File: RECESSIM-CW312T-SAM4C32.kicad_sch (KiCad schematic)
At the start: 2 parts

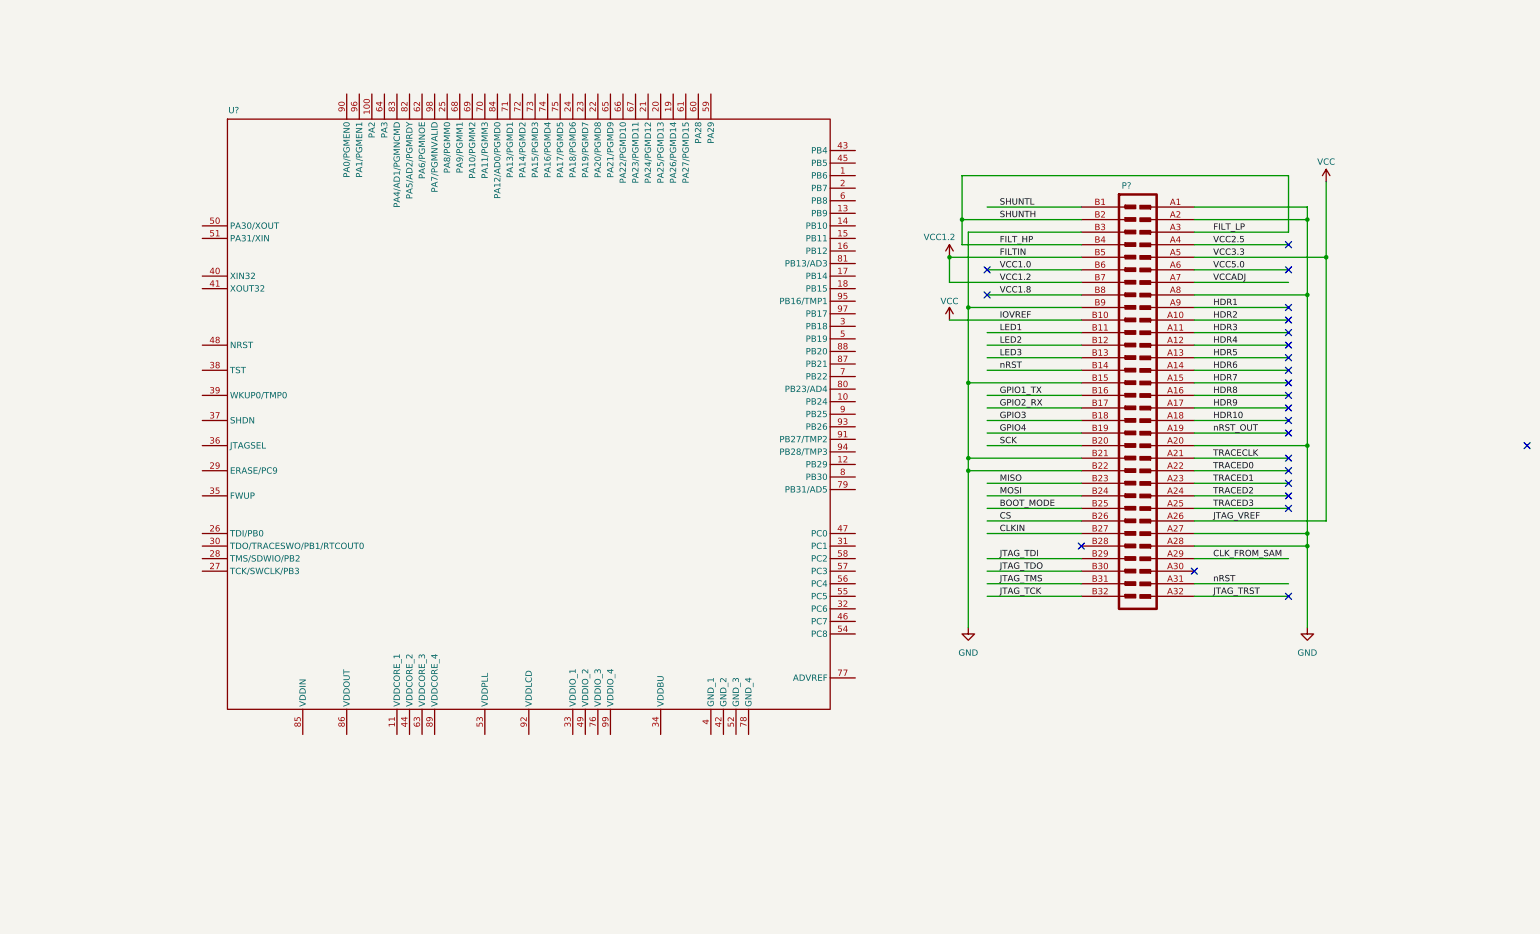
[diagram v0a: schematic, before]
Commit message: Added test points, power and JTAG connections
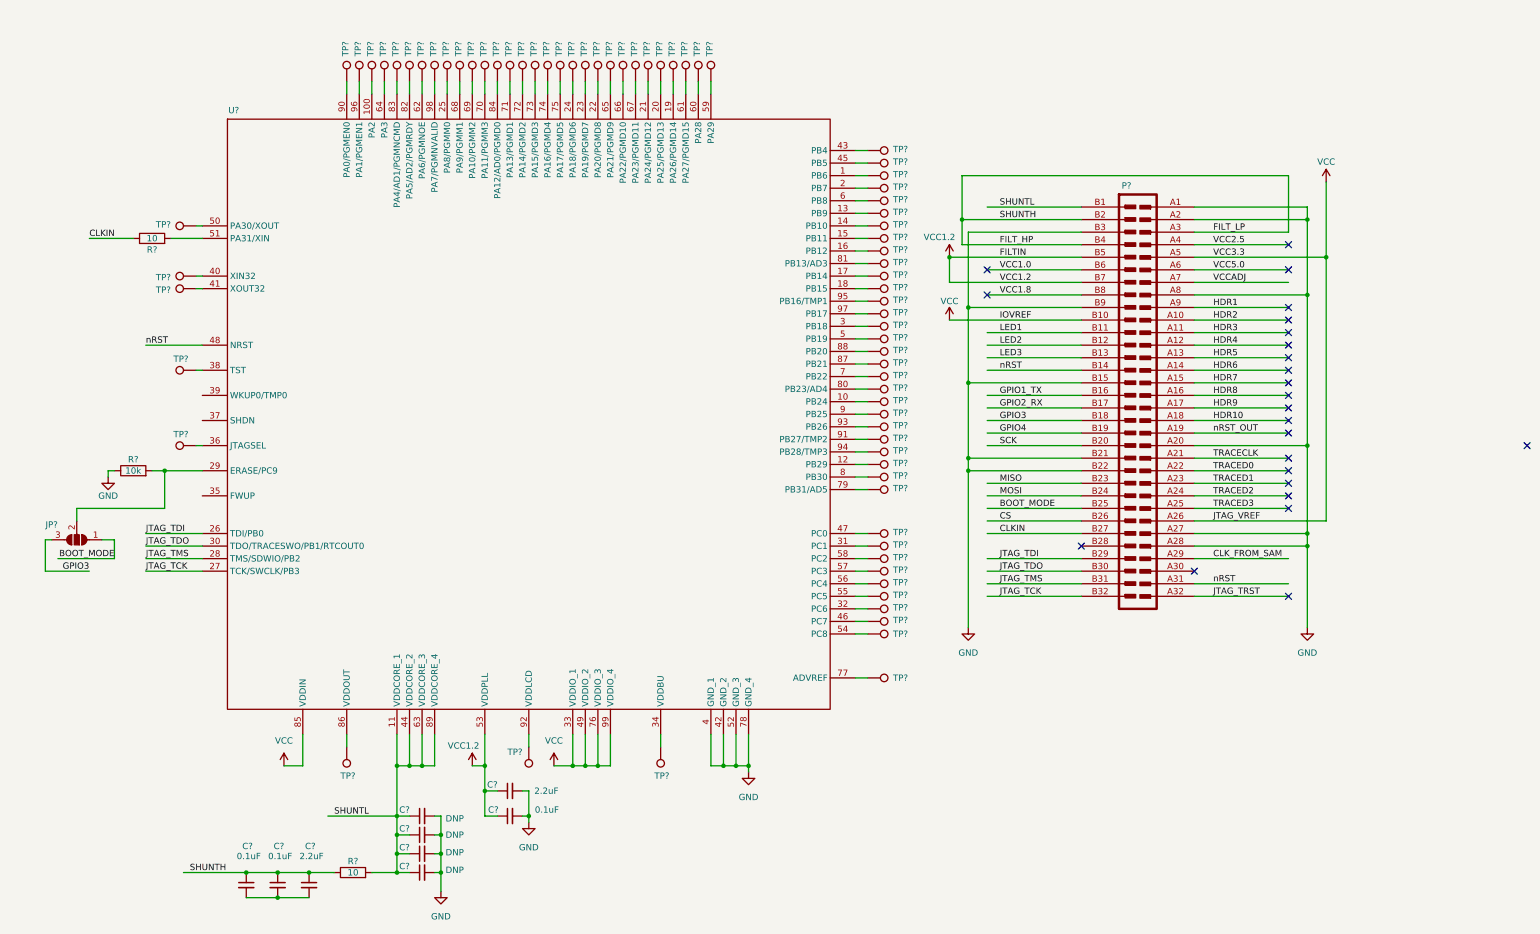
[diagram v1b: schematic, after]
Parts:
- added C? (x3): 0.1uF, symbol Device:C_Small
- added C? (x4): DNP, symbol Device:C_Small
- added C? (x2): 2.2uF, symbol Device:C_Small
- added JP?: SolderJumper_3_Open, symbol Jumper:SolderJumper_3_Open
- added R? (x2): 10, symbol Device:R
- added R?: 10k, symbol Device:R
- added TP? (x76): TestPoint, symbol Connector:TestPoint
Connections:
- net BOOT_MODE: now also JP?.1 (A)
- net CLKIN: now also R?.1
- net FILT_HP: now also C?.1, C?.1, C?.1, R?.1
- net GND: now also U?.4 (GND_1), U?.42 (GND_2), U?.52 (GND_3), U?.78 (GND_4), C?.2, C?.2, C?.2, C?.2, C?.2, C?.2, R?.1
- net GPIO3: now also JP?.3 (B)
- net JTAG_TCK: now also U?.27 (TCK/SWCLK/PB3)
- net JTAG_TDI: now also U?.26 (TDI/PB0)
- net JTAG_TDO: now also U?.30 (TDO/TRACESWO/PB1/RTCOUT0)
- net JTAG_TMS: now also U?.28 (TMS/SDWIO/PB2)
- net SHUNTL: now also U?.11 (VDDCORE_1), U?.44 (VDDCORE_2), U?.63 (VDDCORE_3), U?.89 (VDDCORE_4), C?.1, C?.1, C?.1, C?.1, R?.2
- net VCC: now also U?.33 (VDDIO_1), U?.49 (VDDIO_2), U?.76 (VDDIO_3), U?.85 (VDDIN), U?.99 (VDDIO_4)
- net VCC1.2: now also U?.53 (VDDPLL), C?.1, C?.1
- net nRST: now also U?.48 (NRST)
- net at U?.1 (PB6): now also TP?.1
- net at U?.10 (PB24): now also TP?.1
- net at U?.100 (PA2): now also TP?.1
- net at U?.12 (PB29): now also TP?.1
- net at U?.13 (PB9): now also TP?.1
- net at U?.14 (PB10): now also TP?.1
- net at U?.15 (PB11): now also TP?.1
- net at U?.16 (PB12): now also TP?.1
- net at U?.17 (PB14): now also TP?.1
- net at U?.18 (PB15): now also TP?.1
- net at U?.19 (PA26/PGMD14): now also TP?.1
- net at U?.2 (PB7): now also TP?.1
- net at U?.20 (PA25/PGMD13): now also TP?.1
- net at U?.21 (PA24/PGMD12): now also TP?.1
- net at U?.22 (PA20/PGMD8): now also TP?.1
- net at U?.23 (PA19/PGMD7): now also TP?.1
- net at U?.24 (PA18/PGMD6): now also TP?.1
- net at U?.25 (PA8/PGMM0): now also TP?.1
- net at U?.29 (ERASE/PC9): now also JP?.2 (C), R?.2
- net at U?.3 (PB18): now also TP?.1
- net at U?.31 (PC1): now also TP?.1
- net at U?.32 (PC6): now also TP?.1
- net at U?.34 (VDDBU): now also TP?.1
- net at U?.36 (JTAGSEL): now also TP?.1
- net at U?.38 (TST): now also TP?.1
- net at U?.40 (XIN32): now also TP?.1
- net at U?.41 (XOUT32): now also TP?.1
- net at U?.43 (PB4): now also TP?.1
- net at U?.45 (PB5): now also TP?.1
- net at U?.46 (PC7): now also TP?.1
- net at U?.47 (PC0): now also TP?.1
- net at U?.5 (PB19): now also TP?.1
- net at U?.50 (PA30/XOUT): now also TP?.1
- net at U?.51 (PA31/XIN): now also R?.2
- net at U?.54 (PC8): now also TP?.1
- net at U?.55 (PC5): now also TP?.1
- net at U?.56 (PC4): now also TP?.1
- net at U?.57 (PC3): now also TP?.1
- net at U?.58 (PC2): now also TP?.1
- net at U?.59 (PA29): now also TP?.1
- net at U?.6 (PB8): now also TP?.1
- net at U?.60 (PA28): now also TP?.1
- net at U?.61 (PA27/PGMD15): now also TP?.1
- net at U?.62 (PA6/PGMNOE): now also TP?.1
- net at U?.64 (PA3): now also TP?.1
- net at U?.65 (PA21/PGMD9): now also TP?.1
- net at U?.66 (PA22/PGMD10): now also TP?.1
- net at U?.67 (PA23/PGMD11): now also TP?.1
- net at U?.68 (PA9/PGMM1): now also TP?.1
- net at U?.69 (PA10/PGMM2): now also TP?.1
- net at U?.7 (PB22): now also TP?.1
- net at U?.70 (PA11/PGMM3): now also TP?.1
- net at U?.71 (PA13/PGMD1): now also TP?.1
- net at U?.72 (PA14/PGMD2): now also TP?.1
- net at U?.73 (PA15/PGMD3): now also TP?.1
- net at U?.74 (PA16/PGMD4): now also TP?.1
- net at U?.75 (PA17/PGMD5): now also TP?.1
- net at U?.77 (ADVREF): now also TP?.1
- net at U?.79 (PB31/AD5): now also TP?.1
- net at U?.8 (PB30): now also TP?.1
- net at U?.80 (PB23/AD4): now also TP?.1
- net at U?.81 (PB13/AD3): now also TP?.1
- net at U?.82 (PA5/AD2/PGMRDY): now also TP?.1
- net at U?.83 (PA4/AD1/PGMNCMD): now also TP?.1
- net at U?.84 (PA12/AD0/PGMD0): now also TP?.1
- net at U?.86 (VDDOUT): now also TP?.1
- net at U?.87 (PB21): now also TP?.1
- net at U?.88 (PB20): now also TP?.1
- net at U?.9 (PB25): now also TP?.1
- net at U?.90 (PA0/PGMEN0): now also TP?.1
- net at U?.91 (PB27/TMP2): now also TP?.1
- net at U?.92 (VDDLCD): now also TP?.1
- net at U?.93 (PB26): now also TP?.1
- net at U?.94 (PB28/TMP3): now also TP?.1
- net at U?.95 (PB16/TMP1): now also TP?.1
- net at U?.96 (PA1/PGMEN1): now also TP?.1
- net at U?.97 (PB17): now also TP?.1
- net at U?.98 (PA7/PGMNVALID): now also TP?.1
- new net: C?.2, C?.2, C?.2

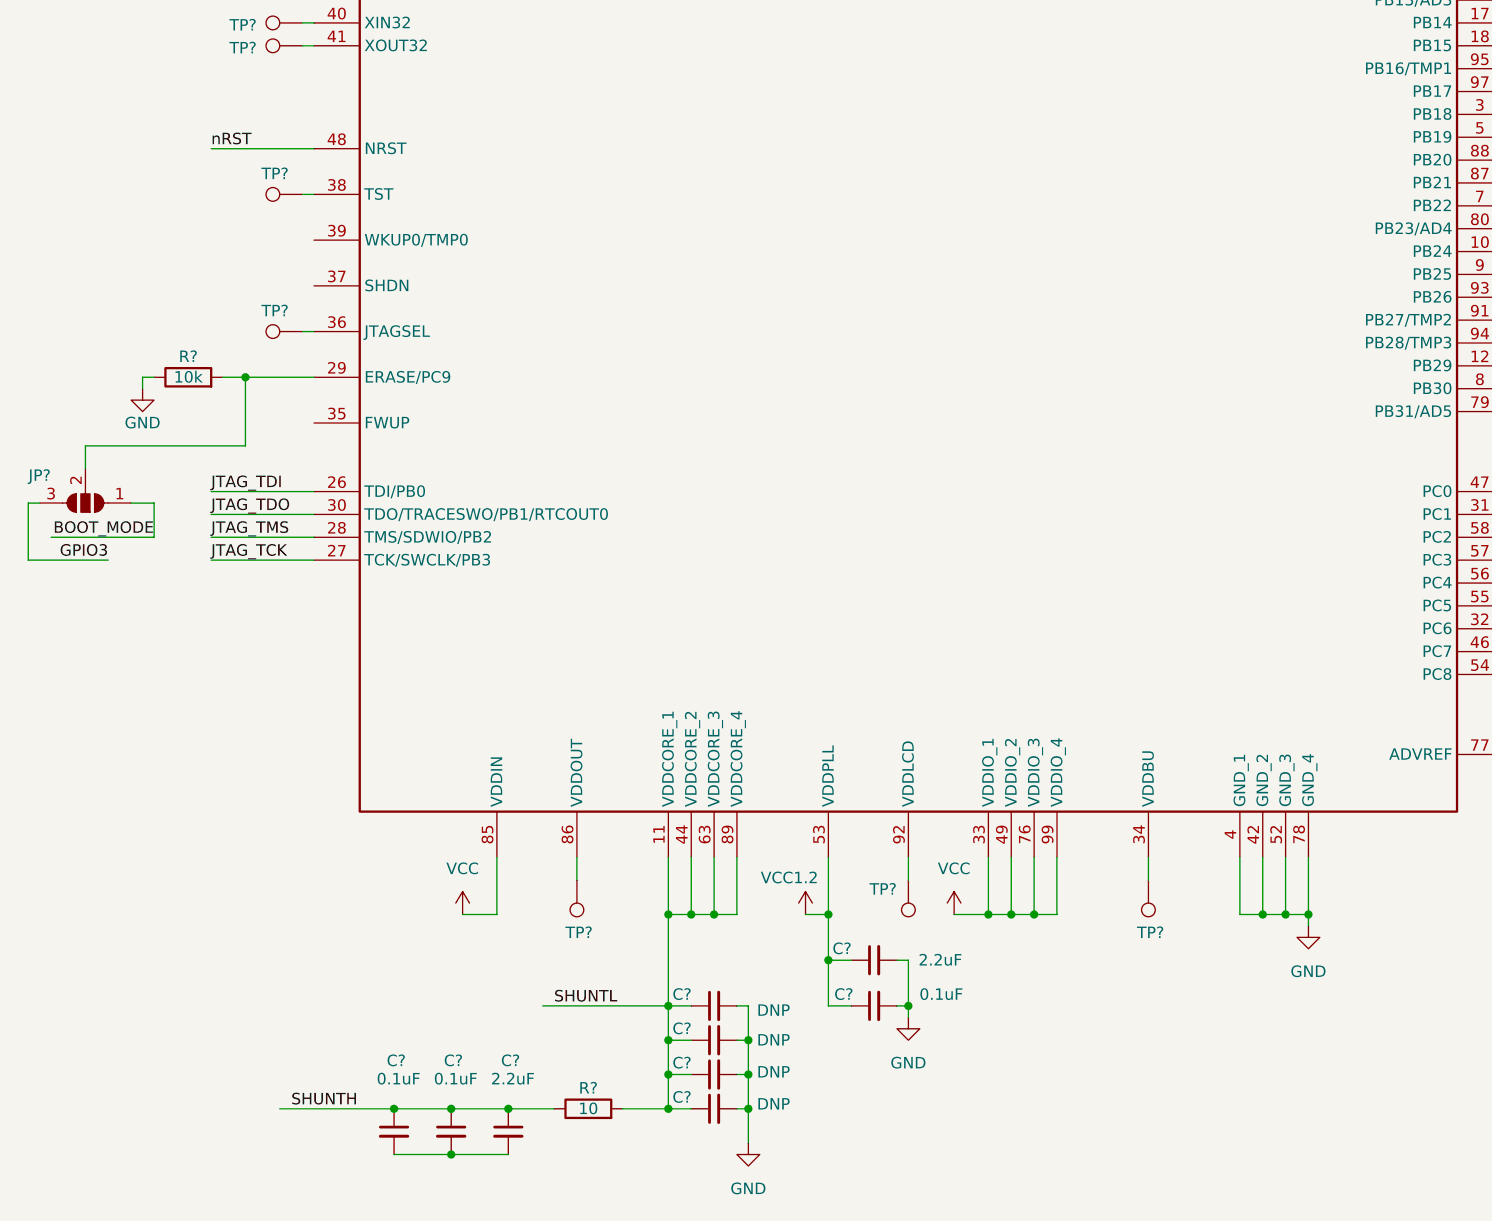
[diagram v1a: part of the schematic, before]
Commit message: Connected VDDBU to power, added more test points
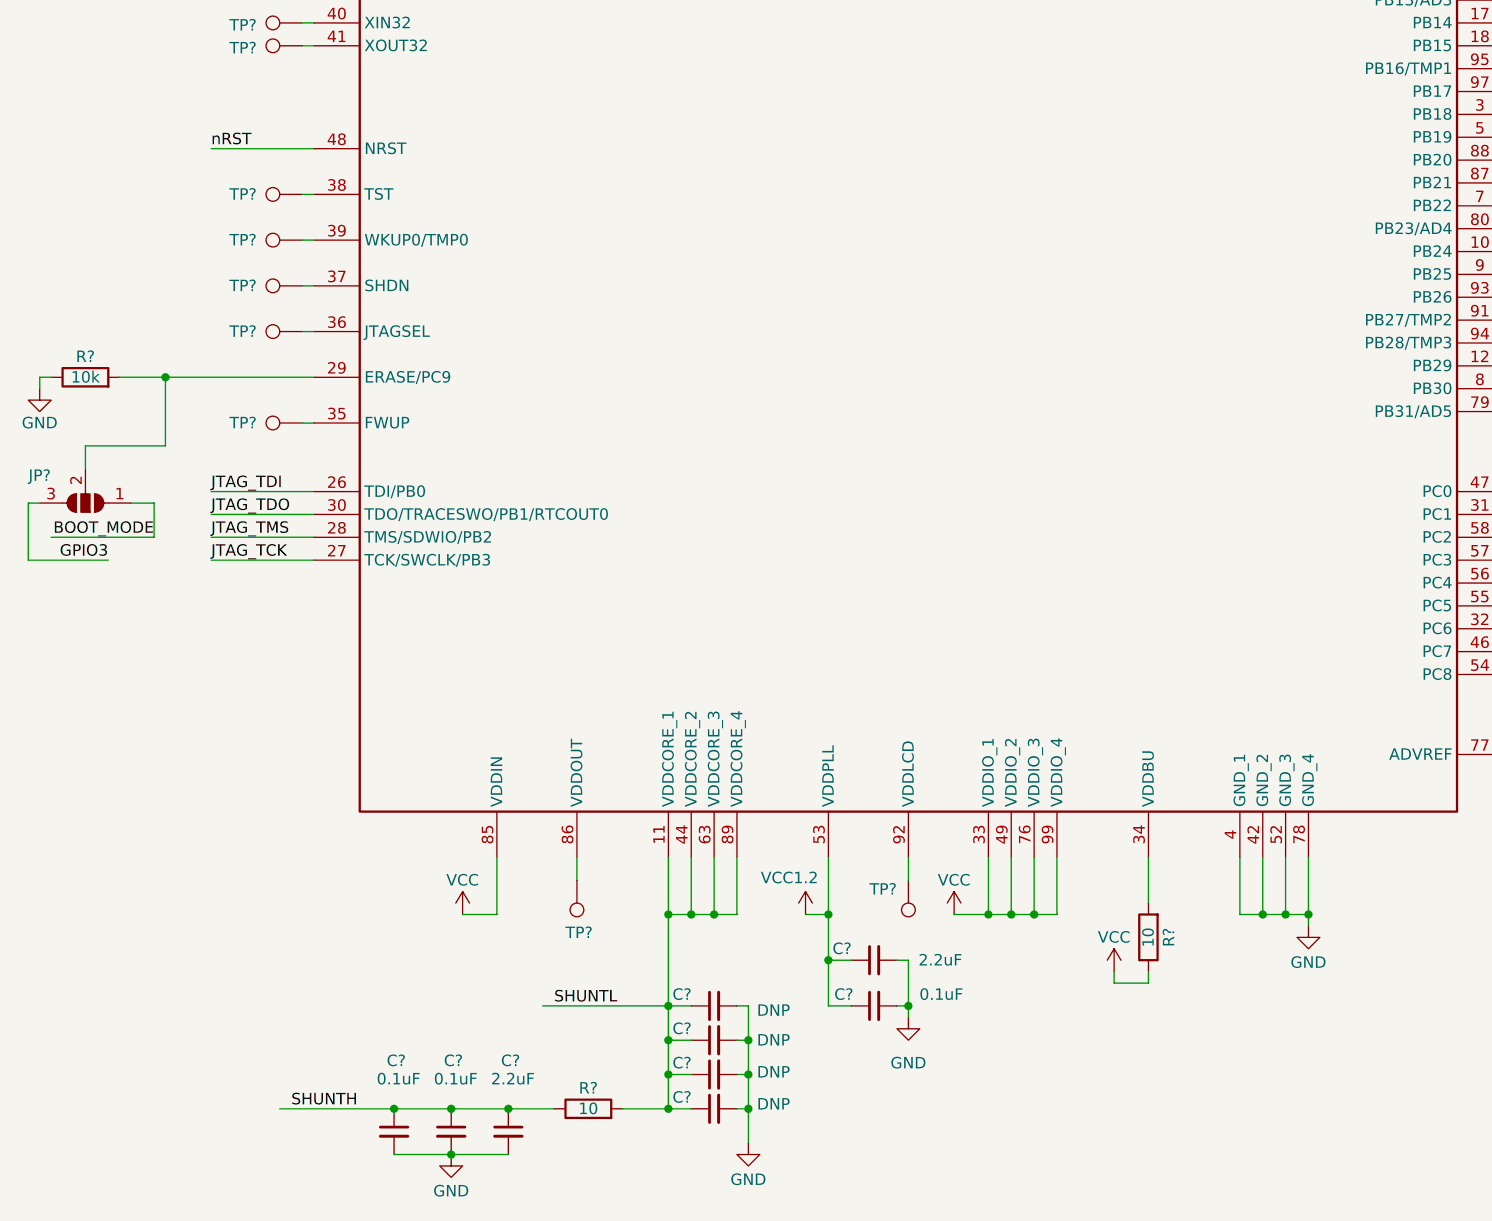
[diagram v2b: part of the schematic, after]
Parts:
- removed TP?: TestPoint, symbol Connector:TestPoint
- added R?: 10, symbol Device:R
- added TP? (x3): TestPoint, symbol Connector:TestPoint
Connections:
- net GND: now also C?.2, C?.2, C?.2
- net VCC: now also R?.1
- net at U?.34 (VDDBU): now also R?.2
- net at U?.35 (FWUP): now also TP?.1
- net at U?.37 (SHDN): now also TP?.1
- net at U?.39 (WKUP0/TMP0): now also TP?.1
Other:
- moved on the sheet: R?

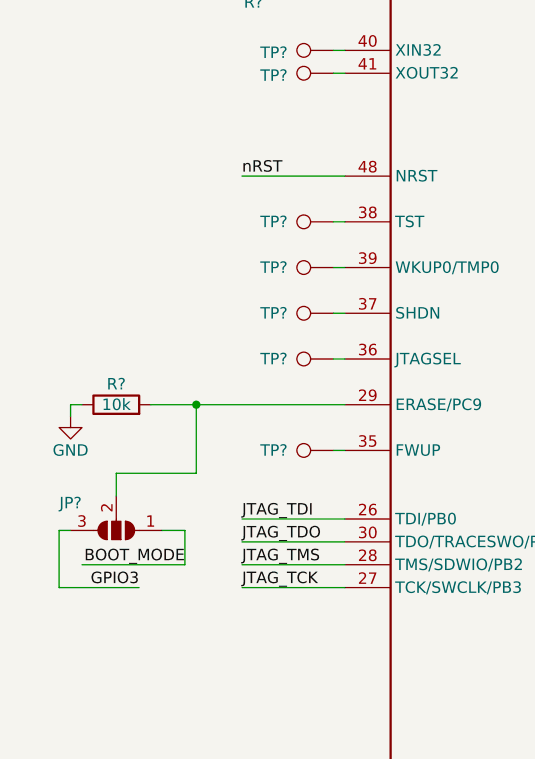
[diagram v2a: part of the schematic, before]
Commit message: Added more test points
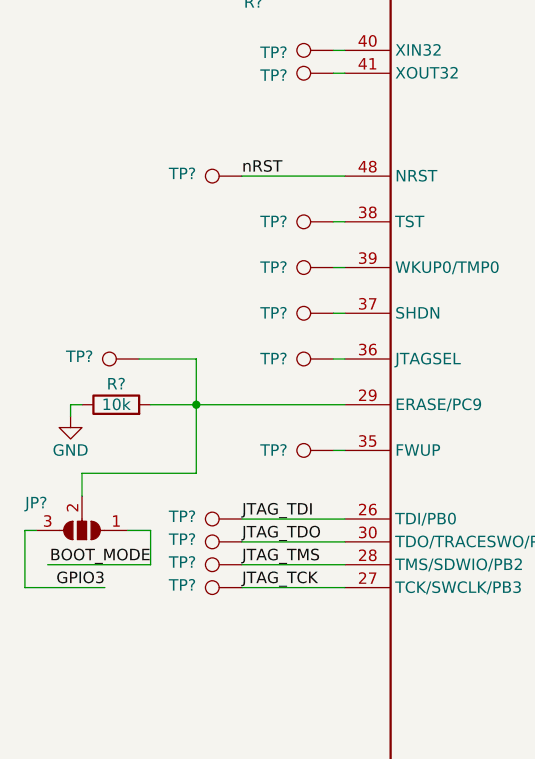
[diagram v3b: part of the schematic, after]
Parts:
- added TP? (x6): TestPoint, symbol Connector:TestPoint
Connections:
- net JTAG_TCK: now also TP?.1
- net JTAG_TDI: now also TP?.1
- net JTAG_TDO: now also TP?.1
- net JTAG_TMS: now also TP?.1
- net nRST: now also TP?.1
- net at JP?.2 (C), R?.2, U?.29 (ERASE/PC9): now also TP?.1
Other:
- moved on the sheet: JP?
